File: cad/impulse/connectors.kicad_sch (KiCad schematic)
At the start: 25 parts, among them J1 Screw_Terminal_01x02, J2 Screw_Terminal_01x02, J3 Screw_Terminal_01x02, J4 Screw_Terminal_01x02, J5 Screw_Terminal_01x02, J6 Screw_Terminal_01x02, J7 Conn_01x08, J8 Conn_01x08, J9 Conn_01x08, Q1 Q_NMOS_DGS, Q3 Q_NMOS_DGS, Q4 Q_NMOS_DGS, Q5 Q_NMOS_DGS

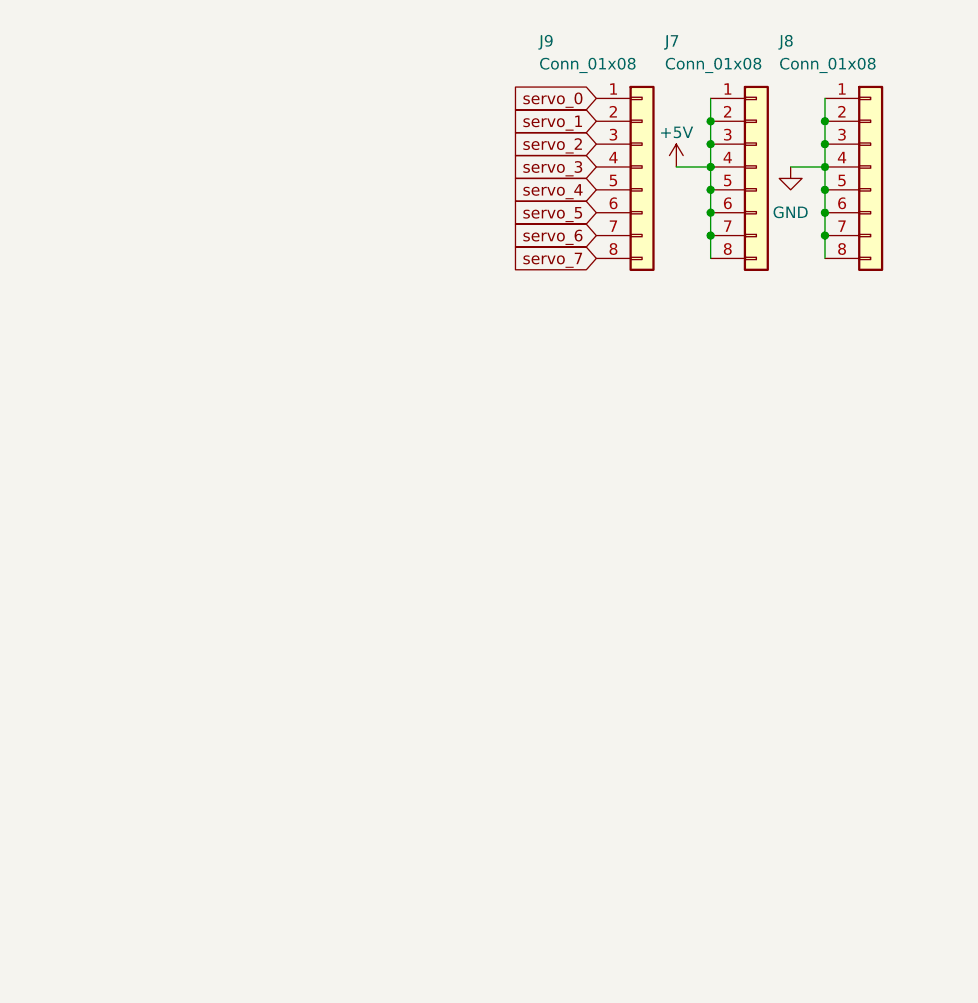
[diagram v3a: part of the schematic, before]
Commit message: Added USB connector.
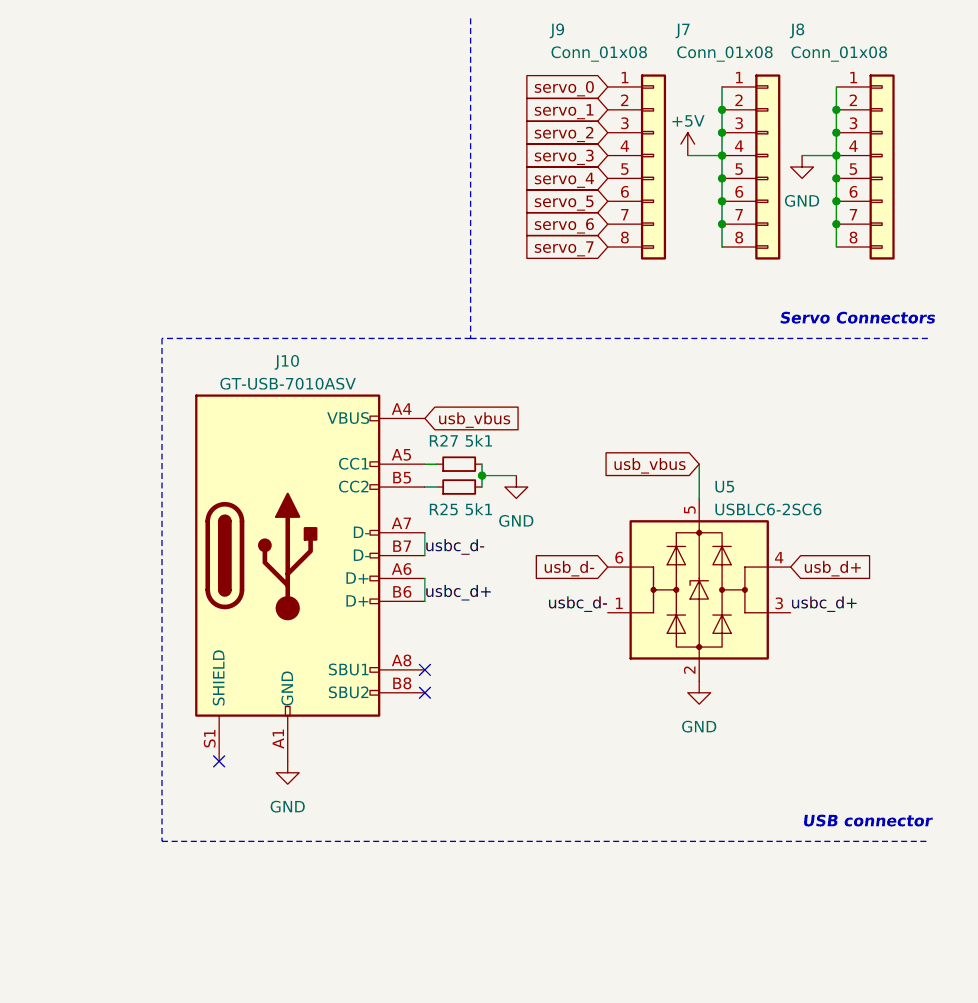
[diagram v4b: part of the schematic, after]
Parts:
- added J10: GT-USB-7010ASV, symbol Connector:USB_C_Receptacle_USB2.0
- added R25, R27: 5k1, symbol Device:R_Small
- added U5: USBLC6-2SC6, Package_TO_SOT_SMD:SOT-23-6, symbol Power_Protection:USBLC6-2SC6
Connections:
- net GND: now also J10.A1 (GND), J10.A12 (GND), J10.B1 (GND), J10.B12 (GND), R25.2, R27.2, U5.2 (GND)
- new net: J10.B5 (CC2), R25.1
- new net: J10.A5 (CC1), R27.1
- new net usb_d+: U5.4 (I/O2)
- new net usb_d-: U5.6 (I/O1)
- new net usb_vbus: J10.A4 (VBUS), J10.A9 (VBUS), J10.B4 (VBUS), J10.B9 (VBUS), U5.5 (VBUS)
- new net usbc_d+: J10.A6 (D+), J10.B6 (D+), U5.3 (I/O2)
- new net usbc_d-: J10.A7 (D-), J10.B7 (D-), U5.1 (I/O1)
- no-connect marks 0 -> 3
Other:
- note added: "Servo Connectors"
- note added: "USB connector"
- moved on the sheet: J7, J8, J9

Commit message: Finished with LoRa.
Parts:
- renumbered D4 to D3, D5 to D4, D6 to D5, J5 to J10, J6 to J2, J9 to J3, J7 to J4, J8 to J5, J2 to J6, J10 to J7, J3 to J8, J4 to J9, Q1 to Q2, R11 to R10, R10 to R11, R13 to R12, R12 to R13, R15 to R14, R14 to R15, R9 to R6, R8 to R7, R27 to R8, R25 to R9, U5 to U3

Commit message: Finnished the design.
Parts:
- removed J3, J4, J5: Conn_01x08, Connector_RJ:RJ45_Amphenol_54602-x08_Horizontal, symbol Connector_Generic:Conn_01x08
- removed Q2, Q3, Q4, Q5: Q_NMOS_DGS, symbol Device:Q_NMOS_DGS
- removed R14, R15: R_Small, symbol Device:R_Small
- added H1, H2, H3, H4: M3, symbol Mechanical:MountingHole_Pad
- added J13: Conn_01x10, symbol Connector_Generic:Conn_01x10
- added J3, J4, J5: Conn_01x06, symbol Connector_Generic:Conn_01x06
- added R33: 665r, symbol Device:R_Small
- added R34: 4k7, symbol Device:R_Small
- added U10, U11, U12, U9: LN2324DT2AG, symbol impulse:LN2324DT2AG
- D2, D3, D4, D5: value D_Small -> 1N4007W
- J1, J10, J2, J6, J8, J9: value Screw_Terminal_01x02 -> DB125-2.54
- R10, R12, R6: value R_Small -> 665r
- R11, R13, R7: value R_Small -> 4k7
- U3: footprint Package_TO_SOT_SMD:SOT-23-6 -> (none)
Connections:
- net +5V: now also J4.1 (Pin_1), J4.2 (Pin_2), J4.3 (Pin_3), J4.4 (Pin_4), J4.5 (Pin_5), J4.6 (Pin_6)
- net GND: now also R11.2, R13.2, R7.2, H1.1, H2.1, H3.1, H4.1, J13.3 (Pin_3), J13.6 (Pin_6), J13.8 (Pin_8), J5.1 (Pin_1), J5.2 (Pin_2), J5.3 (Pin_3), J5.4 (Pin_4), J5.5 (Pin_5), J5.6 (Pin_6), R34.2, U10.4 (S), U11.4 (S), U12.4 (S), U9.4 (S); no longer R11.1, R13.1, R7.1
- net pyro_0: now also R33.2, R34.1; no longer R6.2, R7.2
- net pyro_1: now also R6.2, R7.1; no longer R10.2, R11.2
- net pyro_2: now also R10.2, R11.1; no longer R12.2, R13.2
- net pyro_3: now also R12.2, R13.1
- net servo_0: now also J3.1 (Pin_1)
- net servo_1: now also J3.2 (Pin_2)
- net servo_2: now also J3.3 (Pin_3)
- net servo_3: now also J3.4 (Pin_4)
- net servo_4: now also J3.5 (Pin_5)
- net servo_5: now also J3.6 (Pin_6)
- net at R12.1: now also U12.3 (G)
- net at R10.1: now also U11.3 (G)
- net at R6.1: now also U10.3 (G)
- net pyroOut0 renamed pyro_drain_0
- net pyro_drain_0: now also U9.1 (D), U9.2 (D), U9.5 (D), U9.6 (D)
- net pyroOut1 renamed pyro_drain_1
- net pyro_drain_1: now also U10.1 (D), U10.2 (D), U10.5 (D), U10.6 (D)
- net pyroOut2 renamed pyro_drain_2
- net pyro_drain_2: now also U11.1 (D), U11.2 (D), U11.5 (D), U11.6 (D)
- net pyroOut3 renamed pyro_drain_3
- net pyro_drain_3: now also U12.1 (D), U12.2 (D), U12.5 (D), U12.6 (D)
- new net: R33.1, U9.3 (G)
- new net fpc_gpio: J13.7 (Pin_7)
- new net fpc_rx: J13.4 (Pin_4)
- new net fpc_scl: J13.1 (Pin_1)
- new net fpc_sda: J13.2 (Pin_2)
- new net fpc_tx: J13.5 (Pin_5)
- new net vinp: J13.10 (Pin_10), J13.9 (Pin_9)
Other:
- note added: "FPC connector"
- note added: "Mounting Holes"
- note added: "Pyro Output 0"
- note added: "Pyro Output 1"
- note added: "Pyro Output 2"
- note added: "Pyro Output 3"
- note removed: "Pyro Out 0"
- note removed: "Pyro Out 1"
- note removed: "Pyro Out 2"
- note removed: "Pyro Out 3"
- company: (none) -> markbel
- title: (none) -> Connectors
- moved on the sheet: D2, J6

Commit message: Started working on BOM, did consolidation.
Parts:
- D3: renamed from D2; lcsc (none) -> C2944153
- D4: renamed from D3; lcsc (none) -> C2944153
- D5: renamed from D4; lcsc (none) -> C2944153
- D6: renamed from D5; lcsc (none) -> C2944153
- J10: renamed from J13; lcsc (none) -> C283121
- J8: renamed from J7; lcsc (none) -> C2988369
- R11: renamed from R33; lcsc (none) -> C3015970
- R12: renamed from R34; lcsc (none) -> C103059
- R13: renamed from R8; lcsc (none) -> C3152095
- R14: renamed from R9; lcsc (none) -> C3152095
- R15: renamed from R6; lcsc (none) -> C3015970
- R16: renamed from R7; lcsc (none) -> C103059
- R17: renamed from R10; lcsc (none) -> C3015970
- R18: renamed from R11; lcsc (none) -> C103059
- R19: renamed from R12; lcsc (none) -> C3015970
- R20: renamed from R13; lcsc (none) -> C103059
- U4: renamed from U9; lcsc (none) -> C172432
- U5: renamed from U10; lcsc (none) -> C172432
- U6: renamed from U3; lcsc (none) -> C558442
- U7: renamed from U11; lcsc (none) -> C172432
- U8: renamed from U12; lcsc (none) -> C172432
- renumbered J9 to J11, J10 to J12, J1 to J2, J2 to J3, J3 to J4, J4 to J5, J5 to J6, J6 to J7, J8 to J9

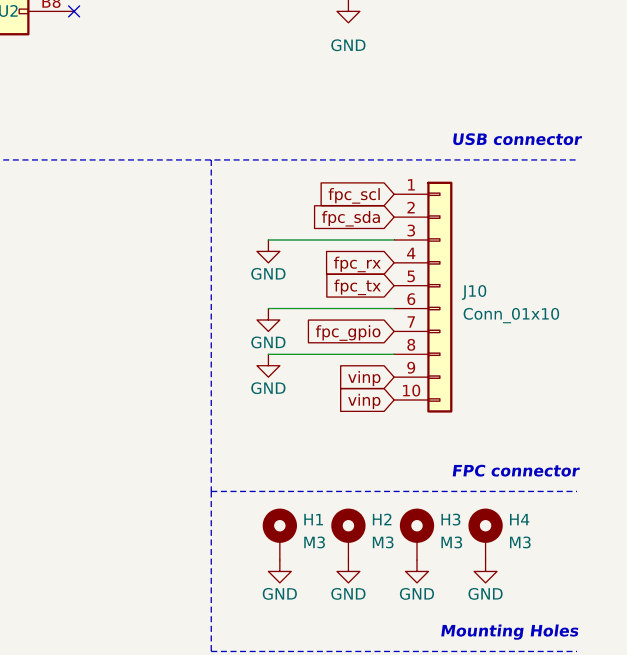
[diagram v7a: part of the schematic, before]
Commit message: Finished with schematic, starting to route traces.
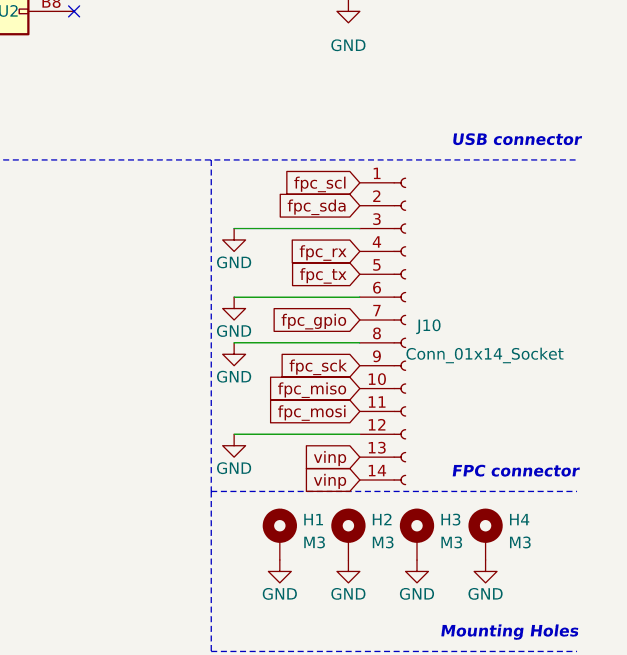
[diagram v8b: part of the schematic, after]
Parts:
- removed J10: Conn_01x10, symbol Connector_Generic:Conn_01x10
- added J10: Conn_01x14_Socket, Connector_FFC-FPC:Hirose_FH12-14S-0.5SH_1x14-1MP_P0.50mm_Horizontal, symbol Connector:Conn_01x14_Socket
- D3, D4, D5, D6: footprint (none) -> Diode_SMD:D_SOD-123F
- H1, H2, H3, H4: footprint (none) -> MountingHole:MountingHole_3.2mm_M3_Pad_Via
- J11, J12, J7, J9: footprint (none) -> TerminalBlock_TE-Connectivity:TerminalBlock_TE_282834-2_1x02_P2.54mm_Horizontal; lcsc (none) -> C918126
- J2, J3: footprint (none) -> TerminalBlock_TE-Connectivity:TerminalBlock_TE_282834-2_1x02_P2.54mm_Horizontal; lcsc (none) -> C918120
- J4, J5, J6: footprint (none) -> Connector_PinHeader_2.54mm:PinHeader_1x06_P2.54mm_Vertical
- J8: footprint (none) -> Connector_USB:USB_C_Receptacle_G-Switch_GT-USB-7010ASV
- R11, R12, R13, R14, R15, R16, R17, R18, R19, R20: footprint (none) -> Resistor_SMD:R_0402_1005Metric
- U4, U5, U7, U8: footprint (none) -> Package_DFN_QFN:DFN-6-L
- U6: footprint (none) -> Package_TO_SOT_SMD:SOT-23-6
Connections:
- net GND: now also J10.12 (Pin_12), J10.3 (Pin_3), J10.6 (Pin_6), J10.8 (Pin_8)
- net fpc_gpio: now also J10.7 (Pin_7)
- net fpc_rx: now also J10.4 (Pin_4)
- net fpc_scl: now also J10.1 (Pin_1)
- net fpc_sda: now also J10.2 (Pin_2)
- net fpc_tx: now also J10.5 (Pin_5)
- net vinp: now also J10.13 (Pin_13), J10.14 (Pin_14)
- new net fpc_miso: J10.10 (Pin_10)
- new net fpc_mosi: J10.11 (Pin_11)
- new net fpc_sck: J10.9 (Pin_9)
